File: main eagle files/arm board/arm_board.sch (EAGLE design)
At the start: 83 parts, among them IC1 OPAMP-DUALU, J1 APPPP45_PCB_HORIZ_RIGHT, J10 APPPP45_PCB_HORIZ_RIGHT, J11 APPPP45_PCB_HORIZ_RIGHT, J12 APPPP45_PCB_HORIZ_RIGHT, J13 APPPP45_PCB_HORIZ_RIGHT, J14 APPPP45_PCB_HORIZ_RIGHT, J15 APPPP45_PCB_HORIZ_RIGHT, J16 APPPP45_PCB_HORIZ_RIGHT, J2 APPPP45_PCB_HORIZ_RIGHT, J3 APPPP45_PCB_HORIZ_RIGHT, J4 APPPP45_PCB_HORIZ_RIGHT, J5 APPPP45_PCB_HORIZ_RIGHT, J6 APPPP45_PCB_HORIZ_RIGHT, J7 APPPP45_PCB_HORIZ_RIGHT, J8 APPPP45_PCB_HORIZ_RIGHT, J9 APPPP45_PCB_HORIZ_RIGHT, Q1 Q_IRF7437SMD, U1 TIVA-1294, U2 XBEE_802.15.4SMD

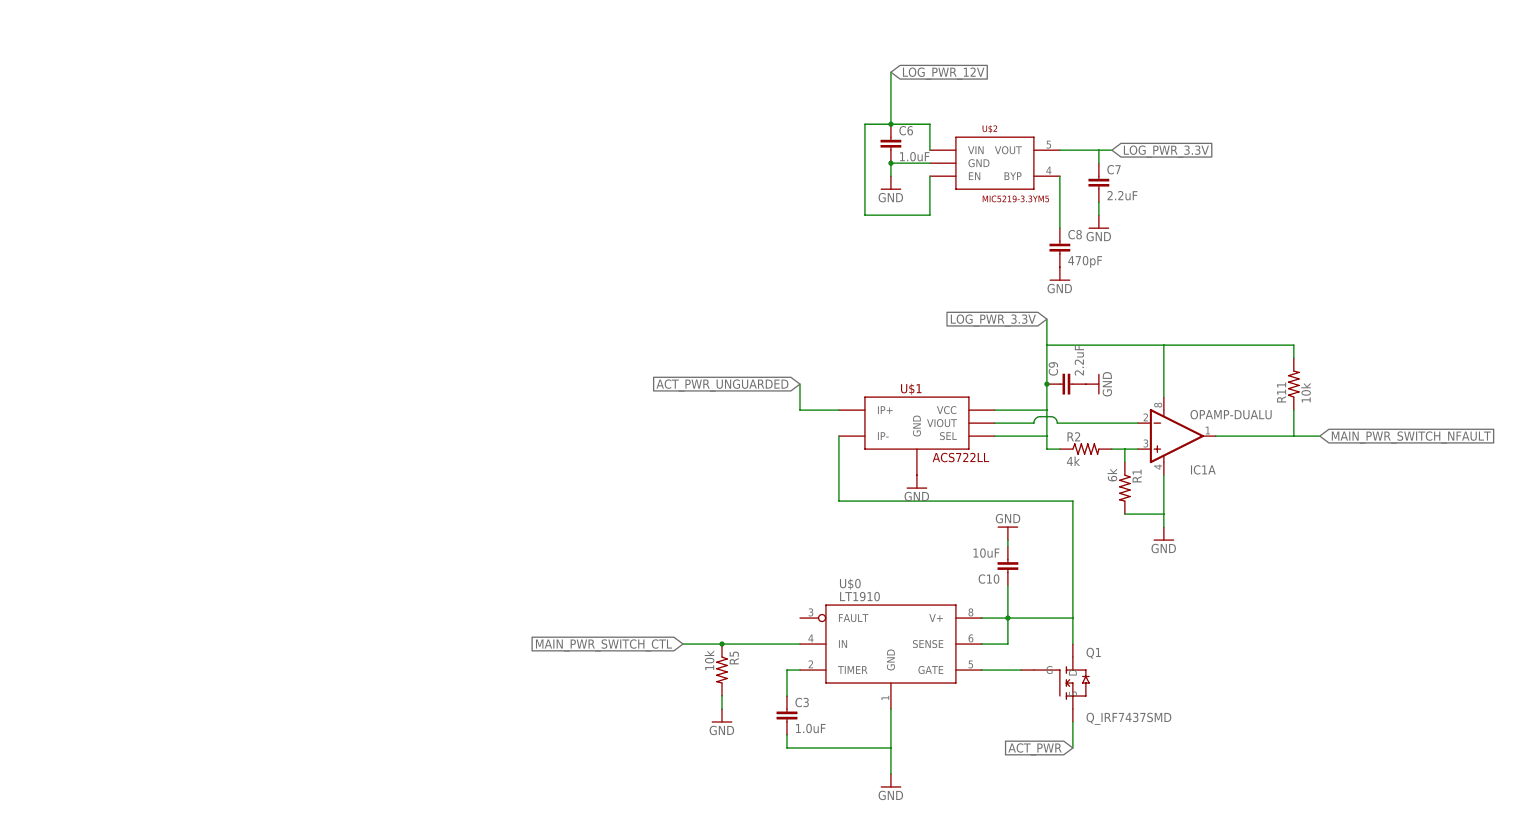
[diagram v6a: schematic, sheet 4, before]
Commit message: Downsized board, added 2 more layers
Went for 4 layers in order to be able to halve the board size, was able
to move the H bridge ic's and connectors much closer while preserving
the ground plane thanks to moving signals to two separate planes.
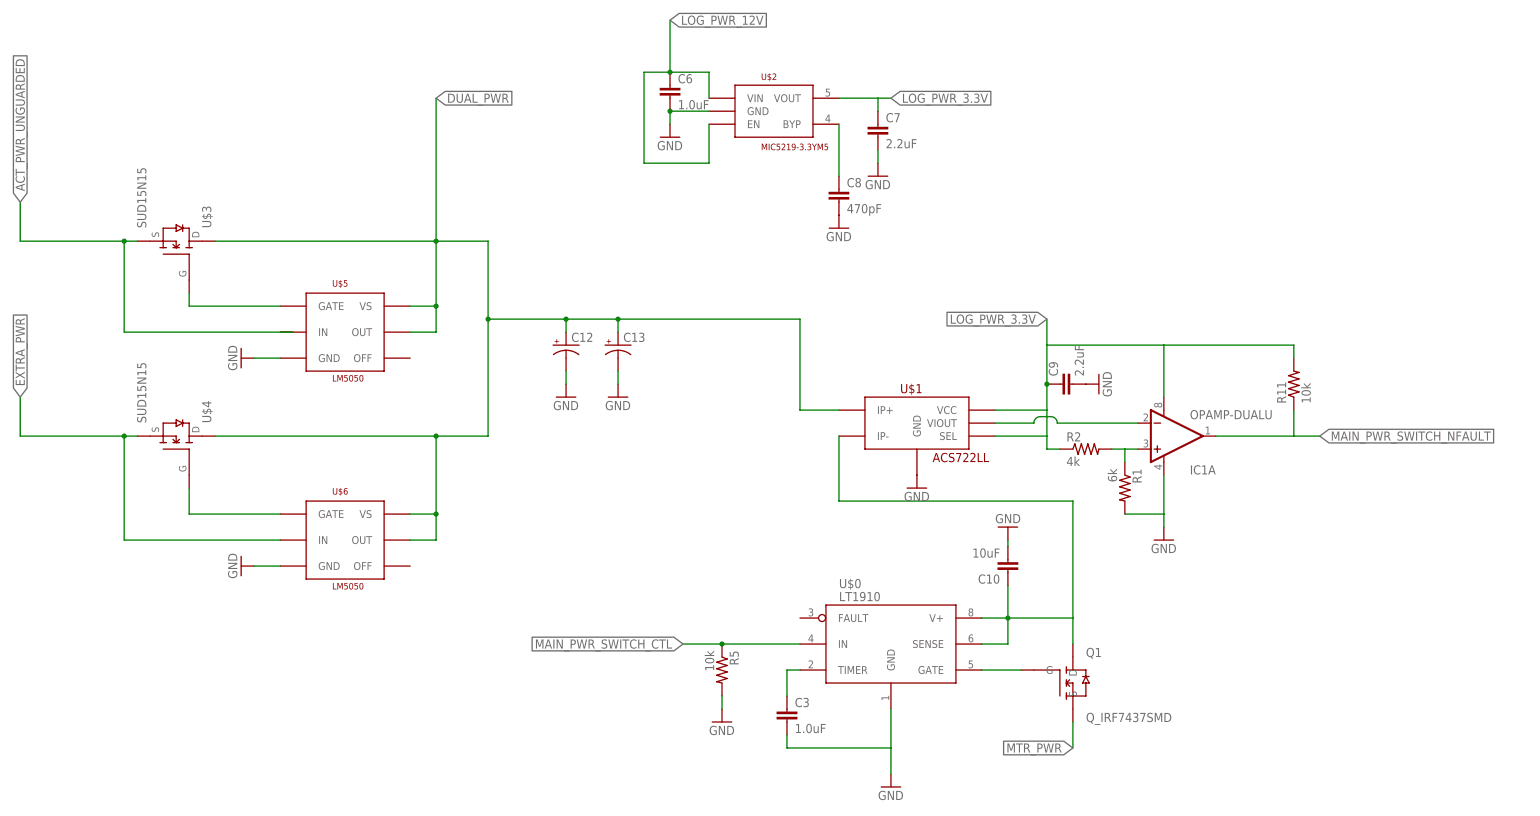
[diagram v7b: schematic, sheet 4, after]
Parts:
- added C11: 2.2uF, SparkFun-Capacitors:2.2UF-CERCAP-10009
- added C12, C13: (no value), SparkFun-Capacitors:CAP_POLC
- added J17, J18: APPPP45_PCB_HORIZ_RIGHT, MRDT-Connectors:APPPP45_PCB_HORIZ_RIGHT
- added U$3, U$4: SUD15N15, mine:SUD15N15
- added U$5, U$6: LM5050, mine:LM5050
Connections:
- net ACT_PWR renamed MTR_PWR
- new net DUAL_PWR: C12.+, C13.+, J16.P$1, U$1.IP+, U$3.D, U$4.D, U$5.OUT, U$5.VS, U$6.OUT, U$6.VS
- new net EXTRA_PWR: C11.1, J18.P$1, U$4.S, U$6.IN
- new net N$11: U$4.G, U$6.GATE
- new net N$8: U$3.G, U$5.GATE
- net ACT_PWR_UNGUARDED: now also U$3.S; no longer J16.P$1, U$1.IP+
- net GND: now also C11.2, C12.-, C13.-, J17.P$1, U$5.GND, U$6.GND
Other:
- moved on the sheet: C1, C2, C6, C7, C8, J1, J2, J3, U$2

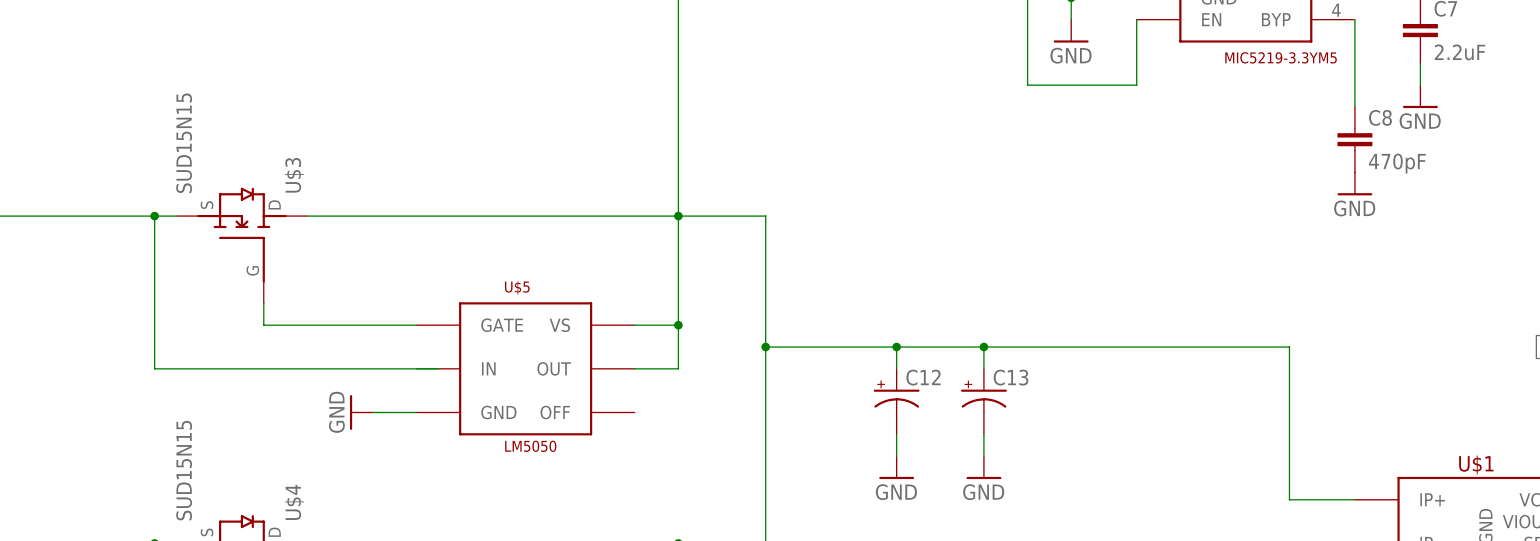
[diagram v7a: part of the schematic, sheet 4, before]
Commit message: U$5 Power OR switcher was missing an input wire
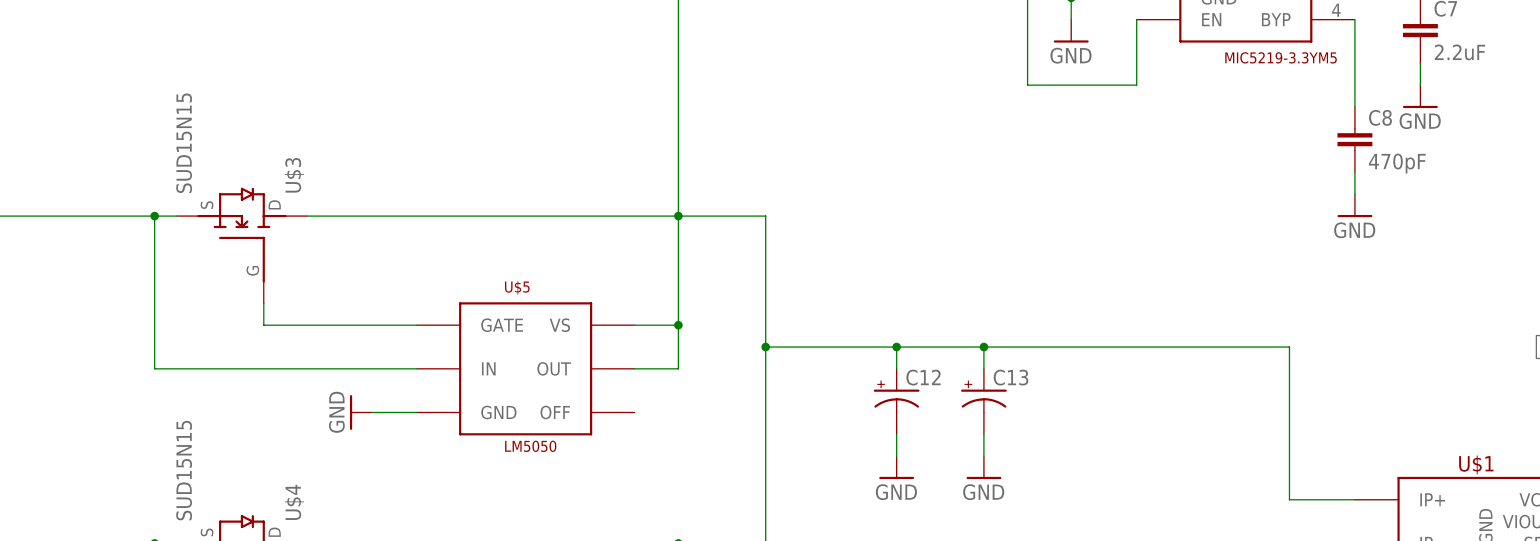
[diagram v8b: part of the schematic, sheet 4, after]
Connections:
- net ACT_PWR_UNGUARDED: now also U$5.IN
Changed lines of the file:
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@@
 <instance part="C8" gate="G$1" x="-12.7" y="20.32"/>
 <instance part="GND20" gate="1" x="-5.08" y="25.4"/>
-<instance part="GND21" gate="1" x="-12.7" y="15.24"/>
+<instance part="GND21" gate="1" x="-12.7" y="12.7"/>
 <instance part="U$0" gate="G$1" x="-2.54" y="-73.66"/>
 <instance part="C3" gate="G$1" x="-22.86" y="-81.28"/>
@@
 <pinref part="C8" gate="G$1" pin="2"/>
 <pinref part="GND21" gate="1" pin="GND"/>
+<wire x1="-12.7" y1="15.24" x2="-12.7" y2="17.78" width="0.1524" layer="91"/>
 </segment>
 <segment>
@@
 <wire x1="-152.4" y1="12.7" x2="-172.72" y2="12.7" width="0.1524" layer="91"/>
 <wire x1="-172.72" y1="12.7" x2="-172.72" y2="20.32" width="0.1524" layer="91"/>
-<wire x1="-119.38" y1="-5.08" x2="-152.4" y2="-5.08" width="0.1524" layer="91"/>
+<wire x1="-121.92" y1="-5.08" x2="-152.4" y2="-5.08" width="0.1524" layer="91"/>
 <wire x1="-152.4" y1="-5.08" x2="-152.4" y2="12.7" width="0.1524" layer="91"/>
 <junction x="-152.4" y="12.7"/>
 <label x="-172.72" y="20.32" size="1.778" layer="95" rot="R90" xref="yes"/>
+<pinref part="U$5" gate="G$1" pin="IN"/>
 </segment>
 </net>
